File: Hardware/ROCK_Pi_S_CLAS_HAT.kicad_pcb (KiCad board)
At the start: 2 copper layers, 43.2 x 43.2 mm, 64 parts, among them J1 ROCK_Pi_S, J2 DX07S016JA1R1500, J3 U.FL-R-SMT-1, J4 DX07S016JA1R1500, Q1 AO3400A, Q2 AO3400A, U1 BPI-9600, U2 USBLC6-2SC6, U3 MIC5219-3.3YM5, U4 ZED-F9R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

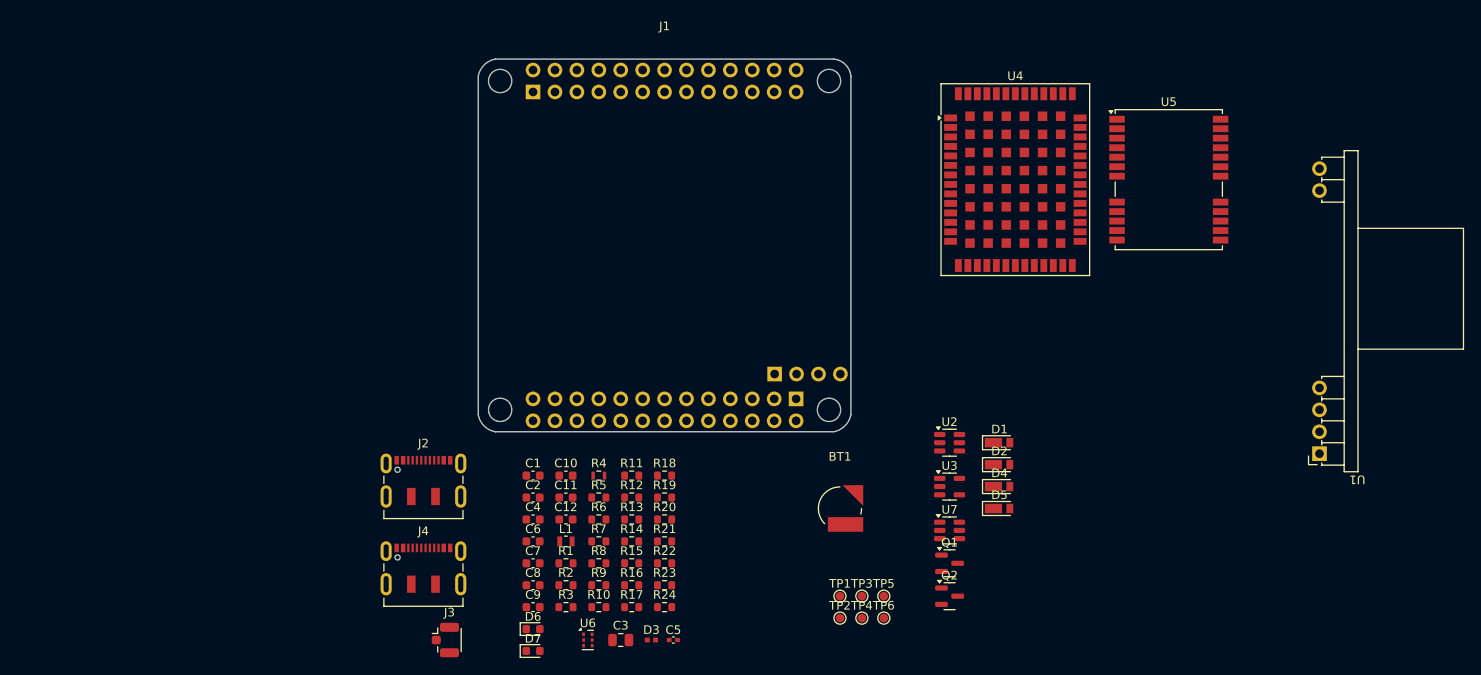
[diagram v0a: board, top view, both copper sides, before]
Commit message: LED追加
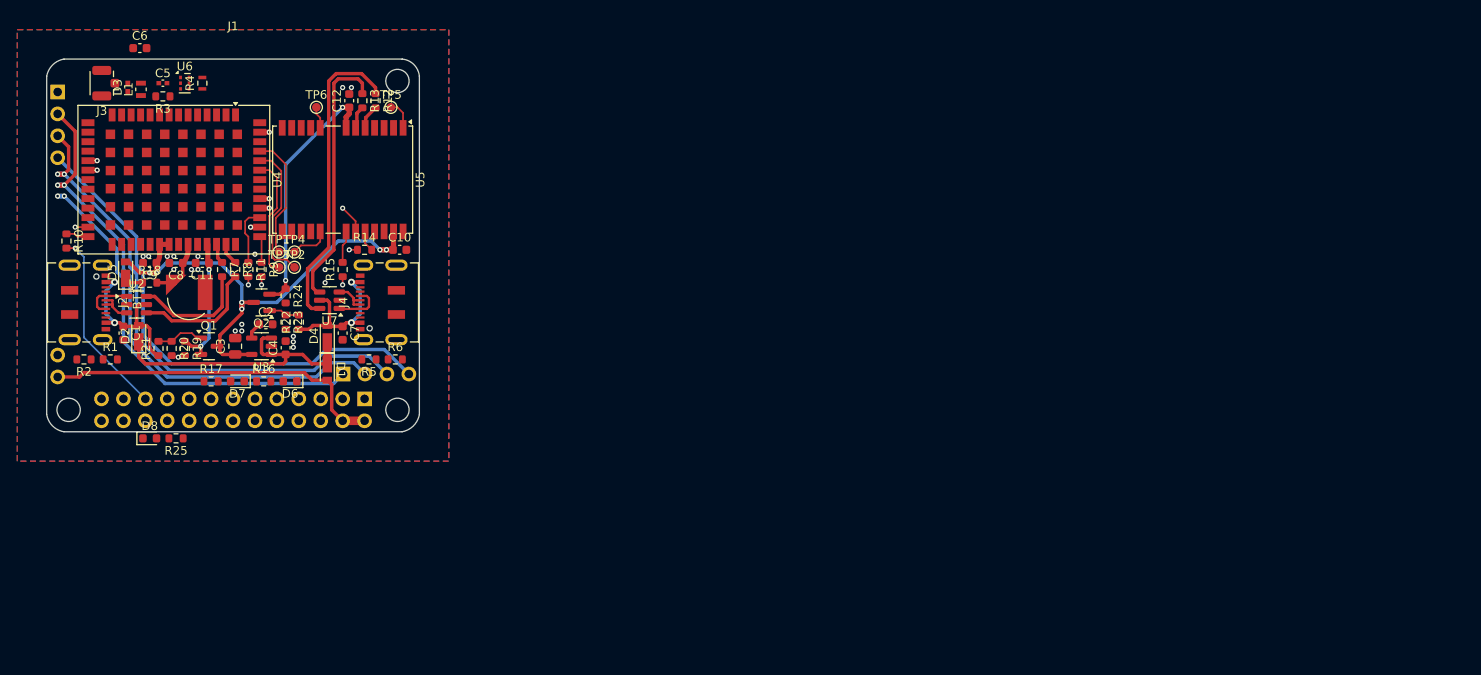
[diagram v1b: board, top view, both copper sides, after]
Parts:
- added D8: PWR(), LED_SMD:LED_0603_1608Metric, F.Cu at (90.3, 122.4)
- added R25: 1k, Resistor_SMD:R_0603_1608Metric, F.Cu at (93.4, 122.4)
- D6: value PULSE -> PULSE()
- D7: value RTK -> RTK()
- U1: moved to B.Cu
- moved U1 152.1 mm to (79.7, 82.2)
- moved D5 104.9 mm to (87.6, 103.1), turned to 90 degrees
- moved D2 100.8 mm to (89.1, 110.5), turned to 90 degrees
- moved U4 97.5 mm to (93.1, 92.4), turned to -90 degrees
- moved U5 95.7 mm to (112.7, 92.4), turned to -90 degrees
- moved U2 95.5 mm to (88.8, 106.9)
- moved Q1 89.4 mm to (97.2, 111.7)
- moved TP6 88.5 mm to (109.7, 84.0)
- moved D3 88.2 mm to (87.8, 81.7), turned to 90 degrees
- moved C5 87.5 mm to (91.9, 81.2)
- moved Q2 86.7 mm to (103.3, 106.6), turned to 180 degrees
- moved U3 81.4 mm to (103.3, 111.7), turned to 180 degrees
- moved TP5 80.4 mm to (118.3, 84.0)
- moved D4 79.8 mm to (110.9, 110.5), turned to 90 degrees
- moved U6 79.6 mm to (94.4, 81.2)
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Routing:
- net Net-(J1C-Pin_54): track 0.00 -> 62.5 mm, vias 0 -> 2
- net Net-(J1C-Pin_53): track 0.00 -> 62.3 mm, vias 0 -> 2
- net Net-(J1C-Pin_55): track 0.00 -> 61.2 mm, vias 0 -> 2
- net +3.3V: track 0.00 -> 59.6 mm, vias 0 -> 6
- net Net-(J1C-Pin_56): track 0.00 -> 58.7 mm
- net Net-(U4-RXD2): track 0.00 -> 42.1 mm, vias 0 -> 2
- net +5V: track 0.00 -> 39.8 mm
- net /SDA1: track 0.00 -> 39.6 mm, vias 0 -> 2
- net /SCL1: track 0.00 -> 37.5 mm, vias 0 -> 2
- net /D-D9C: track 0.00 -> 35.7 mm
- net VDD: track 0.00 -> 33.5 mm
- net /D+D9C: track 0.00 -> 30.7 mm
- net /TXD1_ROCK: track 0.00 -> 30.7 mm, vias 0 -> 1
- net /V_USB_D9C: track 0.00 -> 29.1 mm, vias 0 -> 2
- net /TX_READY_F9R: track 0.00 -> 26.2 mm, vias 0 -> 1
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- added copper zone on B.Cu, net GND
- added copper zone on F.Cu, net GND
- added copper zone on In1.Cu, net GND
- added copper zone on In2.Cu, net GND
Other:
- copper layers 2 -> 4
- board text added: "0"
- board text added: "0 mm"
- board text added: "0.01 mm"
- board text added: "0.0152 mm"
- board text added: "0.02"
- board text added: "0.035 mm"
- board text added: "0.1000 mm / 0.1000 mm"
- board text added: "0.1164 mm"
- board text added: "0.1500 mm"
- board text added: "0.218 mm"
- board text added: "0.4 mm"
- board text added: "0.4mm H/HOZ without copper"
- board text added: "1"
- board text added: "1.6252 mm"
- board text added: "2116 RC54% 4.9mil"
- board text added: "3.3"
- board text added: "4"
- board text added: "4.4"
- board text added: "4.6"
- board text added: "43.1800 mm x 43.1800 mm"
- board text added: "7628, RC 49%, 8.6 mil"
- board text added: "B.Cu"
- board text added: "B.Mask"
- board text added: "B.Paste"
- board text added: "B.Silkscreen"
- board text added: "Bottom Silk Screen"
- board text added: "Bottom Solder Mask"
- board text added: "Bottom Solder Paste"
- board text added: "ENIG"
- board text added: "F.Cu"
- board text added: "F.Mask"
- board text added: "F.Paste"
- board text added: "F.Silkscreen"
- board text added: "In1.Cu"
- board text added: "In2.Cu"
- board text added: "JLC04161H-7628B"
- board text added: "Not specified"
- board text added: "Top Silk Screen"
- board text added: "Top Solder Mask"
- board text added: "Top Solder Paste"
- board text added: "copper"
- board text added: "core"
- board text added: "prepreg"
- board text added: "εR"
- board text added: "いいえ"
- board text added: "はい"
- board text added: "インピーダンス制御:"
- board text added: "エッジ カード コネクタ:"
- board text added: "カラー"
- board text added: "タイプ"
- board text added: "レイヤー名"
- board text added: "基板の特性"
- board text added: "基板全体の寸法:"
- board text added: "基板厚:"
- board text added: "基板端メッキ:"
- board text added: "導体レイヤー数:"
- board text added: "損失正接"
- board text added: "最小穴径:"
- board text added: "最小配線幅/間隔:"
- board text added: "材料"
- board text added: "端面スルーホール パッド:"
- board text added: "線幅 (mm)"
- board text added: "誘電体 1 (1/3)"
- board text added: "誘電体 2"
- board text added: "誘電体 3 (1/3)"
- board text added: "銅箔仕上げ:"

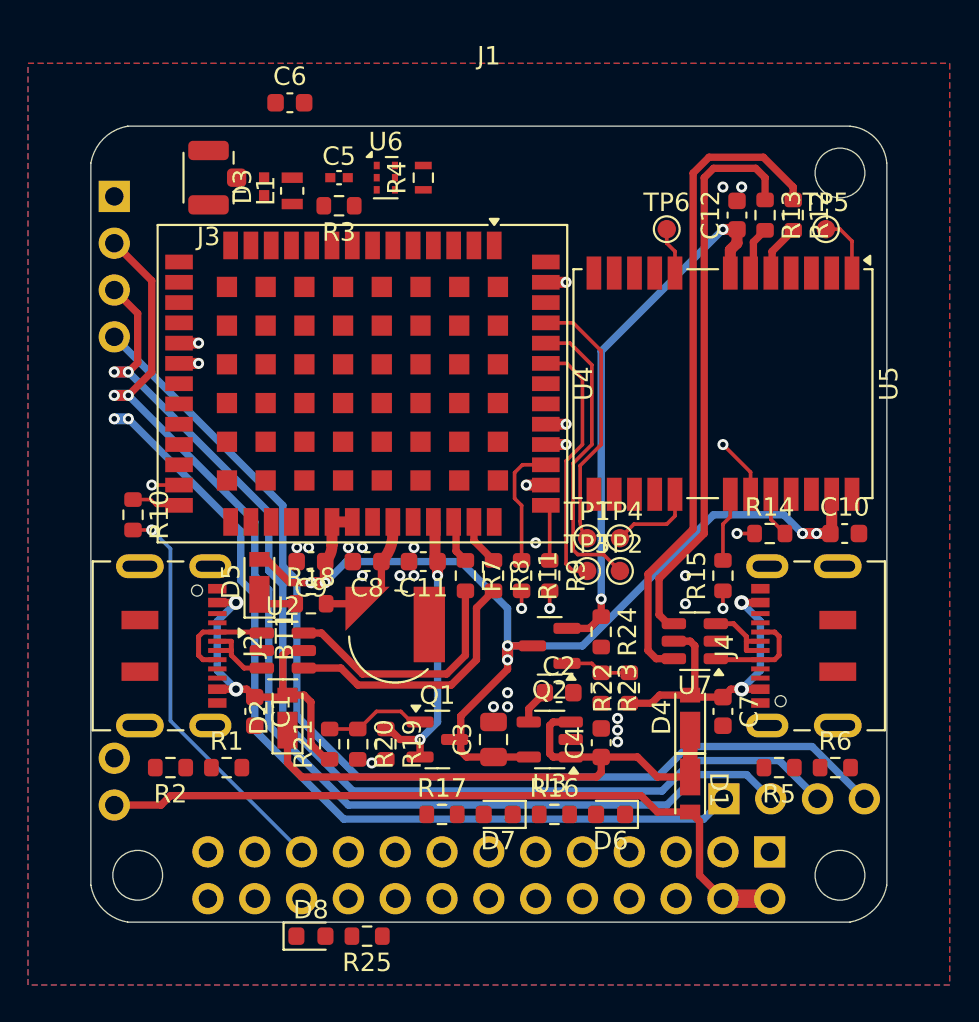
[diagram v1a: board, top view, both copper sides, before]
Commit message: USBコネクタを変更
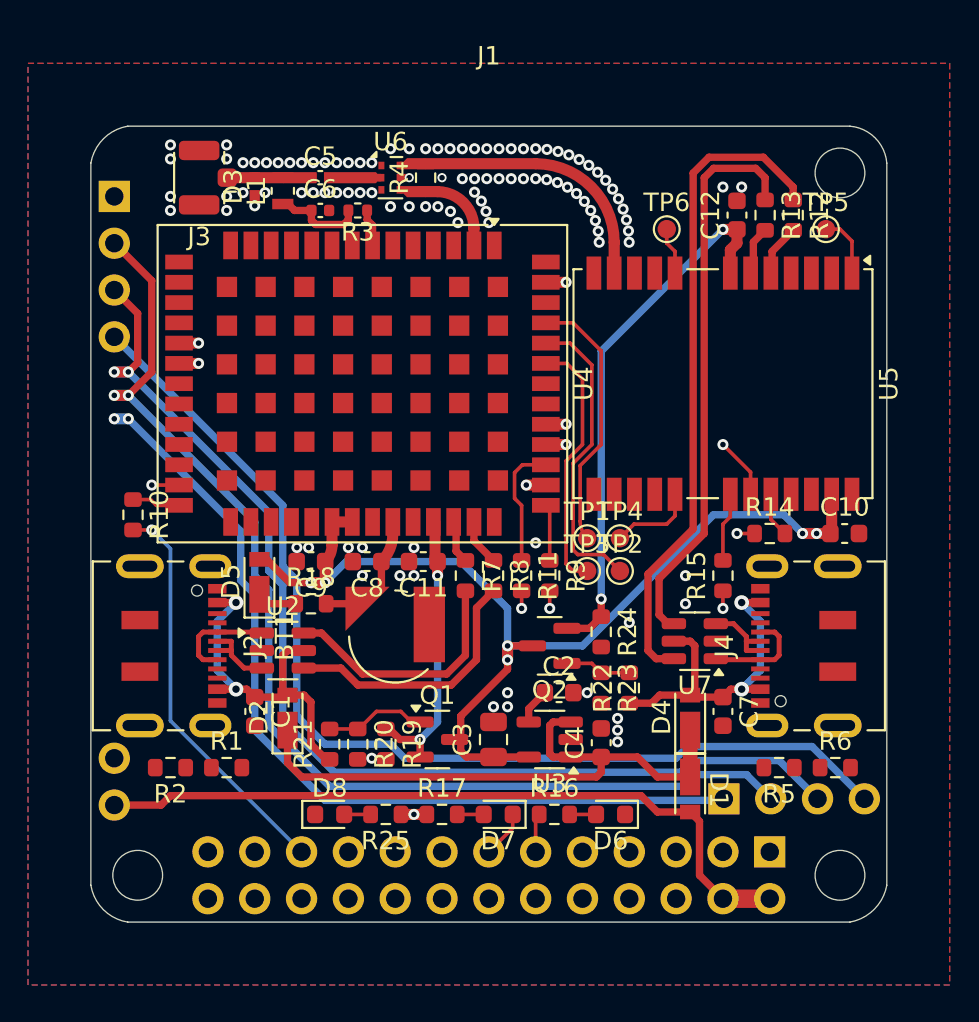
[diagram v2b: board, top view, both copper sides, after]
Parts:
- C6: footprint Capacitor_SMD:C_0603_1608Metric -> Capacitor_SMD:C_0402_1005Metric
- D6: value PULSE() -> PULSE(WHITE)
- D7: value RTK() -> RTK(YELLOW)
- D8: value PWR() -> PWR(RED)
- R3: footprint Resistor_SMD:R_0603_1608Metric -> Resistor_SMD:R_0402_1005Metric
- moved D8 6.68 mm to (91.4, 115.7)
- moved R25 6.68 mm to (94.4, 115.7)
- moved C6 6.07 mm to (90.9, 83.0)
- moved R3 1.05 mm to (92.9, 83.0)
- moved C5 1.02 mm to (90.9, 81.2)
- moved D3 0.51 mm to (87.3, 81.7)
- moved J3 0.51 mm to (84.8, 81.2)
- moved L1 0.51 mm to (88.8, 81.9)
- moved U6 0.25 mm to (94.7, 81.2)
- moved R4 0.13 mm to (96.6, 81.2)
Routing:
- net /RTK: track 1.06 -> 41.7 mm
- net /GEO: track 1.06 -> 41.5 mm
- net /TP: track 1.10 -> 37.6 mm
- net /RF_IN_D9C: track 0.00 -> 14.2 mm
- net +3.3V: track 59.6 -> 72.3 mm, vias 6 -> 7
- net Net-(C6-Pad1): track 0.00 -> 4.94 mm
- net /RF_IN_F9R: track 0.00 -> 4.61 mm
- net Net-(D3-A2): track 0.00 -> 3.01 mm
- net +3.3VA: track 0.00 -> 2.02 mm
- net Net-(D8-A): track 0.00 -> 1.44 mm
- net Net-(D7-A): track 0.00 -> 1.44 mm
- net Net-(D6-A): track 0.00 -> 1.44 mm
- net Net-(J1C-Pin_56): track 58.7 -> 57.8 mm
- net Net-(J1C-Pin_53): track 62.3 -> 61.4 mm
- net Net-(J1C-Pin_54): track 62.5 -> 61.6 mm
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
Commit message: アートワーク設計完了
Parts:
- J2, J4: value DX07S016JA1R1500 -> GT-USB-7025; footprint Connector_USB:USB_C_Receptacle_JAE_DX07S016JA1R1500 -> Connector_USB:USB_C_Receptacle_G-Switch_GT-USB-7025
- moved R1 3.57 mm to (82.2, 113.0), turned to 180 degrees
- moved R2 2.55 mm to (85.3, 113.0), turned to 0 degrees
- moved R5 0.80 mm to (115.0, 113.0)
- moved R6 0.80 mm to (118.0, 113.0)
- moved J2 0.76 mm to (81.5, 106.6)
- moved J4 0.76 mm to (118.5, 106.6)
- moved U7 0.25 mm to (111.2, 106.6)
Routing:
- net Net-(J2-CC1): track 0.00 -> 9.58 mm
- net Net-(J4-CC2): track 0.00 -> 9.43 mm
- net Net-(J2-CC2): track 0.00 -> 6.75 mm
- net Net-(J4-CC1): track 0.00 -> 6.65 mm
- net /VBUS_F9R: track 19.2 -> 22.7 mm
- net /VBUS_D9C: track 18.1 -> 21.4 mm
- net Net-(J2-D+-PadA6): track 4.22 -> 5.99 mm
- net Net-(J4-D+-PadA6): track 4.22 -> 5.92 mm
- net /RTK: track 41.7 -> 40.2 mm
- net /RXD2_ROCK: track 21.8 -> 23.2 mm
- net /V_USB_D9C: track 29.1 -> 30.2 mm
- net Net-(J2-D--PadA7): track 5.69 -> 4.65 mm
- net Net-(J4-D--PadA7): track 5.69 -> 4.76 mm
- net GND: vias 105 -> 282
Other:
- board text added: "CLAS HAT"
- board text added: "PULSE"
- board text added: "PWR"
- board text added: "RTK"
